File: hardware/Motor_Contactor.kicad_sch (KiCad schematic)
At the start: 15 parts

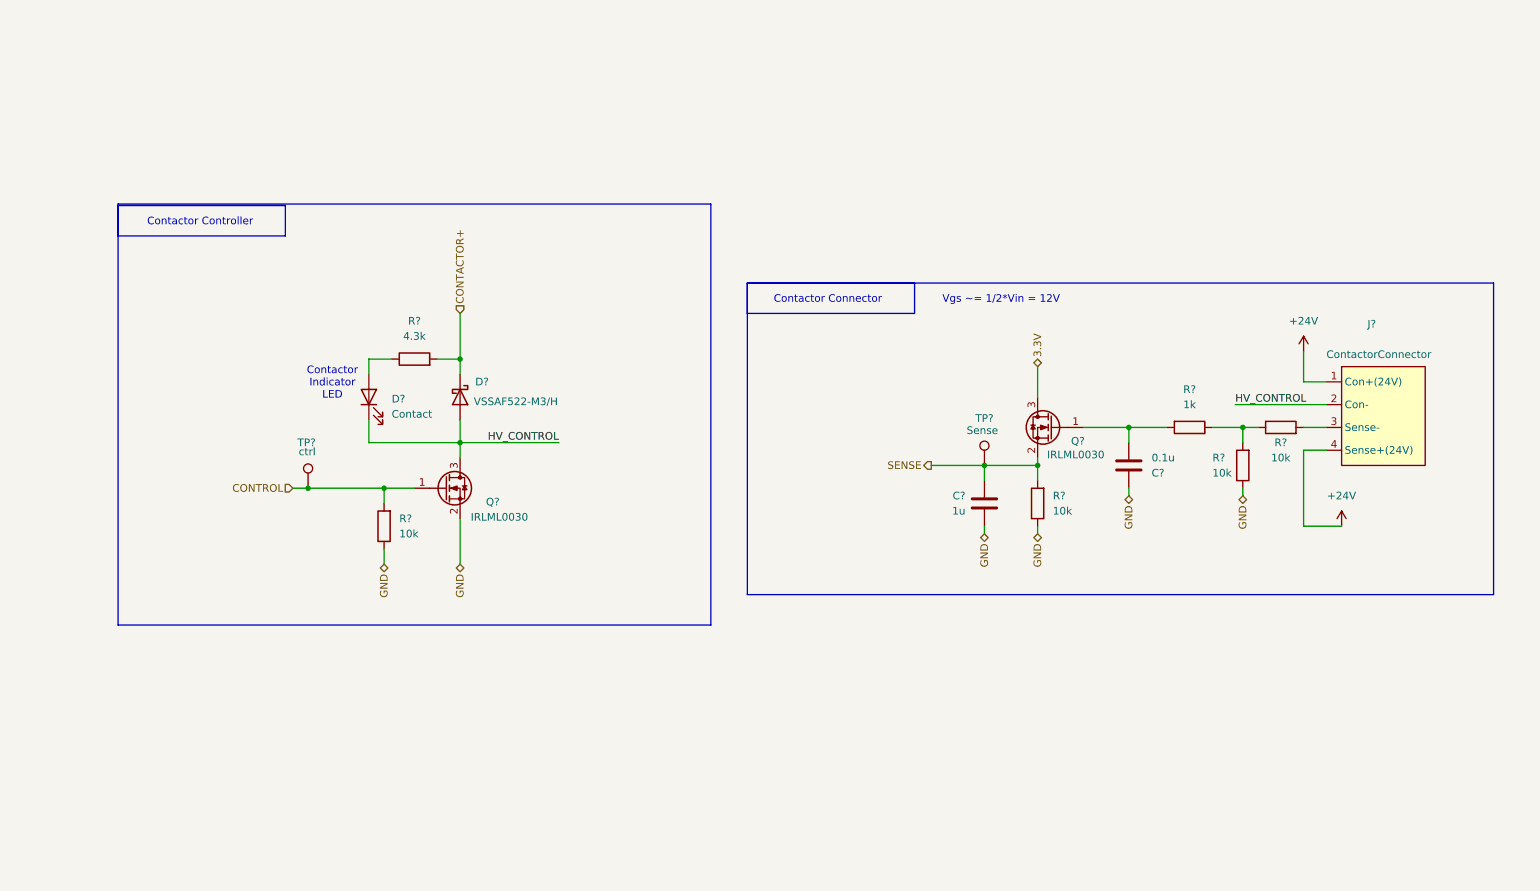
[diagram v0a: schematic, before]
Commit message: new contactor design block, started power mux
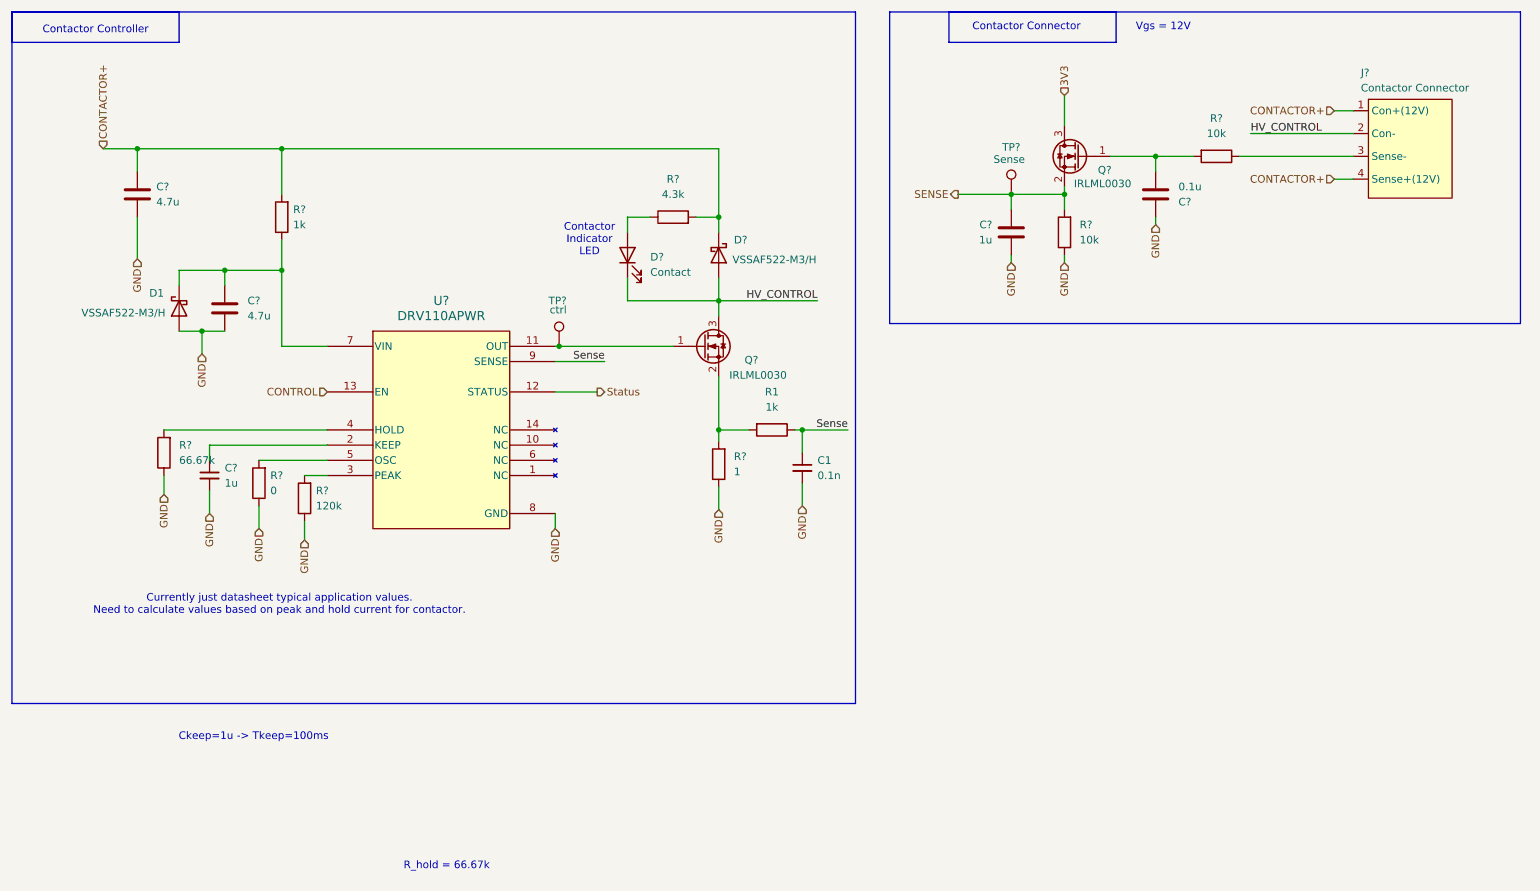
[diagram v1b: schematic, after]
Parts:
- removed C?: 1u, Capacitor_SMD:C_0603_1608Metric_Pad1.08x0.95mm_HandSolder, symbol Device:C
- removed C?: 0.1u, Capacitor_SMD:C_0603_1608Metric_Pad1.08x0.95mm_HandSolder, symbol Device:C
- removed D?: VSSAF522-M3/H, CustomKiCad-Library:SODFL5226X100N, symbol Diode:C3D25170H
- removed D?: Contact, LED_SMD:LED_0603_1608Metric, symbol Device:LED
- removed J?: ContactorConnector, UTSVT_Connectors:Molex_Nano-Fit_105309-xx04_1x04_P2.50mm_Vertical, symbol UTSVT_Connectors:ContactorConnector
- removed Q? (x2): IRLML0030, Package_TO_SOT_SMD:SOT-23, symbol Transistor_FET:IRLML0030
- removed R?: 4.3k, symbol Device:R
- removed R? (x4): 10k, symbol Device:R
- removed R?: 1k, symbol Device:R
- removed TP?: ctrl, TestPoint:TestPoint_Pad_1.0x1.0mm, symbol Connector:TestPoint
- removed TP?: Sense, TestPoint:TestPoint_Pad_1.0x1.0mm, symbol Connector:TestPoint
- added C1: 0.1n, symbol Device:C_Small
- added C? (x2): 4.7u, symbol Device:C
- added C?: 1u, Capacitor_SMD:C_0603_1608Metric_Pad1.08x0.95mm_HandSolder, symbol Device:C
- added C?: 0.1u, Capacitor_SMD:C_0603_1608Metric_Pad1.08x0.95mm_HandSolder, symbol Device:C
- added C?: 1u, symbol Device:C_Small
- added D1, D?: VSSAF522-M3/H, LHRS_Passives:SODFL5226X100N, symbol Diode:C3D25170H
- added D?: Contact, LED_SMD:LED_0603_1608Metric, symbol Device:LED
- added J?: Contactor Connector, LHRS_Connectors:Molex_Nano-Fit_105309-xx04_1x04_P2.50mm_Vertical, symbol lhrs_connectors:ContactorConnector
- added Q? (x2): IRLML0030, Package_TO_SOT_SMD:SOT-23, symbol Transistor_FET:IRLML0030
- added R1, R?: 1k, Resistor_SMD:R_0603_1608Metric_Pad0.98x0.95mm_HandSolder, symbol Device:R
- added R?: 0, Resistor_SMD:R_0603_1608Metric_Pad0.98x0.95mm_HandSolder, symbol Device:R
- added R?: 120k, Resistor_SMD:R_0603_1608Metric_Pad0.98x0.95mm_HandSolder, symbol Device:R
- added R?: 66.67k, Resistor_SMD:R_0603_1608Metric_Pad0.98x0.95mm_HandSolder, symbol Device:R
- added R? (x2): 10k, Resistor_SMD:R_0603_1608Metric_Pad0.98x0.95mm_HandSolder, symbol Device:R
- added R?: 4.3k, Resistor_SMD:R_0603_1608Metric_Pad0.98x0.95mm_HandSolder, symbol Device:R
- added R?: 1, Resistor_SMD:R_0603_1608Metric_Pad0.98x0.95mm_HandSolder, symbol Device:R
- added TP?: ctrl, TestPoint:TestPoint_THTPad_D3.0mm_Drill1.5mm, symbol Connector:TestPoint
- added TP?: Sense, TestPoint:TestPoint_THTPad_D3.0mm_Drill1.5mm, symbol Connector:TestPoint
- added U?: DRV110APWR, PW14_TEX, symbol lhrs_ics:DRV110APWR
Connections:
- net CONTACTOR+: now also C?.1, D?.1 (K), J?.1 (Con+(12V)), J?.4 (Sense+(12V)), R?.2, R?.2
- net CONTROL: now also U?.13 (EN)
- net GND: now also C1.2, C?.1, C?.1, C?.2, C?.2, C?.2, D1.2 (A), R?.1, R?.1, R?.1, R?.1, R?.1, U?.8 (GND)
- net HV_CONTROL: now also D?.1 (K), D?.2 (A), J?.2 (Con-), Q?.3 (D)
- net SENSE: now also C?.2, Q?.2 (S), R?.2, TP?.1
- new net: D?.2 (A), R?.1
- new net: Q?.1 (G), TP?.1, U?.11 (OUT)
- new net: Q?.2 (S), R1.2, R?.2
- new net: R?.2, U?.5 (OSC)
- new net: C?.1, D1.1 (K), R?.1, U?.7 (VIN)
- new net: R?.2, U?.3 (PEAK)
- new net: C?.1, U?.2 (KEEP)
- new net: R?.2, U?.4 (HOLD)
- new net: J?.3 (Sense-), R?.1
- new net: C?.2, Q?.1 (G), R?.2
- new net 3V3: Q?.3 (D)
- new net Sense: C1.1, R1.1, U?.9 (SENSE)
- new net Status: U?.12 (STATUS)
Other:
- note added: "Ckeep=1u -> Tkeep=100ms"
- note added: "Currently just datasheet typical application values. Need to calculate values based on peak and hold current for contactor."
- note added: "R_hold = 66.67k"
- note added: "Vgs = 12V"
- note removed: "Vgs ~= 1/2*Vin = 12V"

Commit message: finished schematic except for 12v buck boost
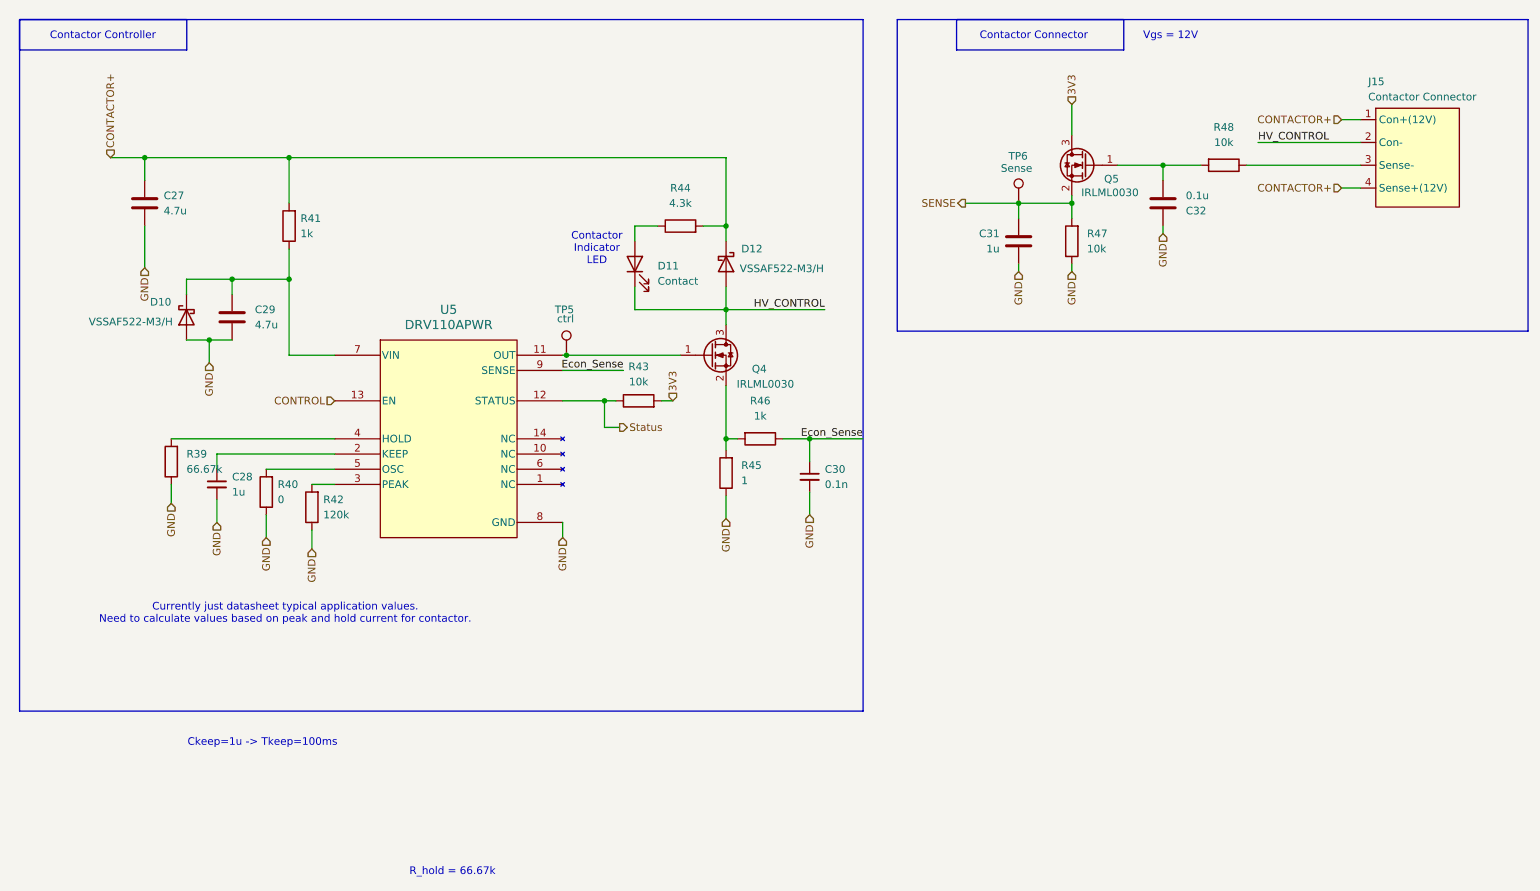
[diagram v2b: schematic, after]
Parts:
- removed C1: 0.1n, symbol Device:C_Small
- removed C? (x2): 4.7u, symbol Device:C
- removed C?: 1u, Capacitor_SMD:C_0603_1608Metric_Pad1.08x0.95mm_HandSolder, symbol Device:C
- removed C?: 0.1u, Capacitor_SMD:C_0603_1608Metric_Pad1.08x0.95mm_HandSolder, symbol Device:C
- removed C?: 1u, symbol Device:C_Small
- removed D1, D?: VSSAF522-M3/H, LHRS_Passives:SODFL5226X100N, symbol Diode:C3D25170H
- removed D?: Contact, LED_SMD:LED_0603_1608Metric, symbol Device:LED
- removed J?: Contactor Connector, LHRS_Connectors:Molex_Nano-Fit_105309-xx04_1x04_P2.50mm_Vertical, symbol lhrs_connectors:ContactorConnector
- removed Q? (x2): IRLML0030, Package_TO_SOT_SMD:SOT-23, symbol Transistor_FET:IRLML0030
- removed R1, R?: 1k, Resistor_SMD:R_0603_1608Metric_Pad0.98x0.95mm_HandSolder, symbol Device:R
- removed R?: 0, Resistor_SMD:R_0603_1608Metric_Pad0.98x0.95mm_HandSolder, symbol Device:R
- removed R?: 120k, Resistor_SMD:R_0603_1608Metric_Pad0.98x0.95mm_HandSolder, symbol Device:R
- removed R?: 66.67k, Resistor_SMD:R_0603_1608Metric_Pad0.98x0.95mm_HandSolder, symbol Device:R
- removed R? (x2): 10k, Resistor_SMD:R_0603_1608Metric_Pad0.98x0.95mm_HandSolder, symbol Device:R
- removed R?: 4.3k, Resistor_SMD:R_0603_1608Metric_Pad0.98x0.95mm_HandSolder, symbol Device:R
- removed R?: 1, Resistor_SMD:R_0603_1608Metric_Pad0.98x0.95mm_HandSolder, symbol Device:R
- removed TP?: ctrl, TestPoint:TestPoint_THTPad_D3.0mm_Drill1.5mm, symbol Connector:TestPoint
- removed TP?: Sense, TestPoint:TestPoint_THTPad_D3.0mm_Drill1.5mm, symbol Connector:TestPoint
- removed U?: DRV110APWR, PW14_TEX, symbol lhrs_ics:DRV110APWR
- added C27, C29: 4.7u, Capacitor_SMD:C_0805_2012Metric_Pad1.18x1.45mm_HandSolder, symbol Device:C
- added C28: 1u, Capacitor_SMD:C_0603_1608Metric_Pad1.08x0.95mm_HandSolder, symbol Device:C_Small
- added C30: 0.1n, Capacitor_SMD:C_0603_1608Metric_Pad1.08x0.95mm_HandSolder, symbol Device:C_Small
- added C31: 1u, Capacitor_SMD:C_0603_1608Metric_Pad1.08x0.95mm_HandSolder, symbol Device:C
- added C32: 0.1u, Capacitor_SMD:C_0603_1608Metric_Pad1.08x0.95mm_HandSolder, symbol Device:C
- added D10, D12: VSSAF522-M3/H, LHRS_Passives:SODFL5226X100N, symbol Diode:C3D25170H
- added D11: Contact, LED_SMD:LED_0603_1608Metric_Pad1.05x0.95mm_HandSolder, symbol Device:LED
- added J15: Contactor Connector, LHRS_Connectors:Molex_Nano-Fit_105309-xx04_1x04_P2.50mm_Vertical, symbol lhrs_connectors:ContactorConnector
- added Q4, Q5: IRLML0030, Package_TO_SOT_SMD:SOT-23, symbol Transistor_FET:IRLML0030
- added R39: 66.67k, Resistor_SMD:R_0603_1608Metric_Pad0.98x0.95mm_HandSolder, symbol Device:R
- added R40: 0, Resistor_SMD:R_0603_1608Metric_Pad0.98x0.95mm_HandSolder, symbol Device:R
- added R41, R46: 1k, Resistor_SMD:R_0603_1608Metric_Pad0.98x0.95mm_HandSolder, symbol Device:R
- added R42: 120k, Resistor_SMD:R_0603_1608Metric_Pad0.98x0.95mm_HandSolder, symbol Device:R
- added R43, R47, R48: 10k, Resistor_SMD:R_0603_1608Metric_Pad0.98x0.95mm_HandSolder, symbol Device:R
- added R44: 4.3k, Resistor_SMD:R_0603_1608Metric_Pad0.98x0.95mm_HandSolder, symbol Device:R
- added R45: 1, Resistor_SMD:R_0603_1608Metric_Pad0.98x0.95mm_HandSolder, symbol Device:R
- added TP5: ctrl, TestPoint:TestPoint_THTPad_D3.0mm_Drill1.5mm, symbol Connector:TestPoint
- added TP6: Sense, TestPoint:TestPoint_THTPad_D3.0mm_Drill1.5mm, symbol Connector:TestPoint
- added U5: DRV110APWR, LHRS_ICs:PW14_TEX, symbol lhrs_ics:DRV110APWR
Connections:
- net 3V3: now also Q5.3 (D), R43.2
- net CONTACTOR+: now also C27.1, D12.1 (K), J15.1 (Con+(12V)), J15.4 (Sense+(12V)), R41.2, R44.2
- net CONTROL: now also U5.13 (EN)
- net GND: now also C27.2, C28.2, C29.2, C30.2, C31.1, C32.1, D10.2 (A), R39.1, R40.1, R42.1, R45.1, R47.1, U5.8 (GND)
- net HV_CONTROL: now also D11.1 (K), D12.2 (A), J15.2 (Con-), Q4.3 (D)
- net SENSE: now also C31.2, Q5.2 (S), R47.2, TP6.1
- net Status: now also R43.1, U5.12 (STATUS)
- new net: J15.3 (Sense-), R48.1
- new net: Q4.1 (G), TP5.1, U5.11 (OUT)
- new net: R39.2, U5.4 (HOLD)
- new net: D11.2 (A), R44.1
- new net: C28.1, U5.2 (KEEP)
- new net: R42.2, U5.3 (PEAK)
- new net: R40.2, U5.5 (OSC)
- new net: C29.1, D10.1 (K), R41.1, U5.7 (VIN)
- new net: C32.2, Q5.1 (G), R48.2
- new net: Q4.2 (S), R45.2, R46.2
- new net Econ_Sense: C30.1, R46.1, U5.9 (SENSE)
